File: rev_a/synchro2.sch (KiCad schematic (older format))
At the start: 26 parts, among them SW1 BUTTON_SPST, U1 AS505X, U2 AS505X, U3 LM2931, U4 MCP2562, U5 TM4C123_QFP64_SYNCHRO2, X1 10MHz

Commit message: Rev. A is pretty close to being ready.
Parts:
- removed N3: JTAG, symbol SWDEBUG_CONN
- added C22, C23: .1uF, symbol C
- added H1: M3.0_#4_HOLE_J, symbol M3.0_#4_HOLE
- added H10, H5: M1.0_HOLE, symbol M1.0_HOLE
- added H2: M3.0_#4_HOLE_K, symbol M3.0_#4_HOLE
- added H3: M3.0_#4_HOLE_L, symbol M3.0_#4_HOLE
- added H4: M3.0_#4_HOLE_M, symbol M3.0_#4_HOLE
- added H6: M3.5_#6_HOLE_N, symbol M3.5_#6_HOLE
- added H7: M3.5_#6_HOLE_O, symbol M3.5_#6_HOLE
- added H8: M3.5_#6_HOLE_P, symbol M3.5_#6_HOLE
- added H9: M3.5_#6_HOLE_Q, symbol M3.5_#6_HOLE
- added J1: UPDATE_ENABLE, symbol EN_DIS_JUMPER
- added N3, N4: ARM_JTAG_10PIN, symbol ARM_JTAG_10PIN
- added TP1: L5.0V, symbol TEST_POINT
- added TP13: MB_TX, symbol TEST_POINT
- added TP14: MB_RX, symbol TEST_POINT
- added TP15: ENC_INT, symbol TEST_POINT
- added TP16: DR_SCLK, symbol TEST_POINT
- added TP17: DR_SEL, symbol TEST_POINT
- added TP18: DR_MISO, symbol TEST_POINT
- added TP19: DR_MOSI, symbol TEST_POINT
- added TP2: L3.3V, symbol TEST_POINT
- added TP3: LGND, symbol TEST_POINT
- C1: value C -> 22uF
- C2, C5, C6, C7, C8: value .1 -> .1uF
- C4: renamed from C3; value .1 -> .1uF
- D1: value LED_VERT -> R971-KN-1
- R2: value R_VERT -> 10K
- SW1: value BUTTON_SPST -> RESET_BUTTON
- U1, U2: value AS505X -> AS5050
- U5: value TM4C123_QFP64_SYNCHRO2 -> TM4C123GH6PM
- U6: renamed from U?; value TC101X -> TC1015
- gave numbers to parts that had none: 1
- renumbered C9 to C11, C11 to C12, C4 to C3
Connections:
- net 3.3V: now also C22.1, C23.1, N3.1 (VCC), N4.1 (VCC), TP2.1 (TESTPOINT)
- net 5V: now also TP1.1 (TESTPOINT)
- net GND: now also C22.2, C23.2, J1.2 (GND), N3.3 (GND), N3.5 (GND), N3.9 (GNDDETECT), N4.3 (GND), N4.5 (GND), N4.9 (GNDDETECT), TP3.1 (TESTPOINT)
- net Motor_Power/MB_PWM_CLK: now also U5.57 (PB5/CAN0Tx/SSI2Fss/T1CCP1); no longer U5.58 (PB4/CAN0Rx/SSI2Clk/T1CCP0)
- net MB_RX: now reaches U5.59 (PE4/CAN0Rx/U5Rx)
- net MB_RX: now also U4.4 (RXD), TP14.1 (TESTPOINT); no longer U4.1 (TXD)
- net MB_TX: now reaches U5.60 (PE5/CAN0Tx/U5Tx)
- net MB_TX: now also U4.1 (TXD), TP13.1 (TESTPOINT); no longer U4.4 (RXD)
- net at U4.8 (STBY): now also U5.58 (PB4/CAN0Rx/SSI2Clk/T1CCP0); no longer U5.24 (PA7)
- net SEL_FB: now reaches U5.43 (PD4/U6Rx/WT4CCP0)
- net SEL_FB: now also N1.14 (SEL1); no longer N1.13 (SEL0)
- net SEL_LR: now reaches U5.44 (PD5/U6Tx/WT4CCP1)
- net SEL_LR: now also N1.13 (SEL0); no longer N1.14 (SEL1)
- net TW_MOSI: now reaches U1.1 (MOSI), U5.22 (PA5/SSI0Tx)
- net at U1.15 (~INT), U5.1 (PB6/SSI2Rx/T0CCP0): now also TP15.1 (TESTPOINT)
- net TW_MISO: now reaches U1.2 (MISO), U5.21 (PA4/SSI0Rx)
- net TW_SCK: now reaches U1.3 (SCK), U5.19 (PA2/SSI0Clk)
- net ~TW_SEL: now reaches U1.4 (~SS), U5.20 (PA3/SSI0Fss)
- net DR_MOSI: now reaches U2.1 (MOSI), U5.29 (PF1/SSI1Tx/T0CCP1/U1CTS)
- net DR_MOSI: now also TP19.1 (TESTPOINT)
- net DR_MISO: now reaches U2.2 (MISO), U5.28 (PF0/CAN0Rx/SSI1Rx/T0CCP0/U1RTS)
- net DR_MISO: now also TP18.1 (TESTPOINT)
- net DR_SCLK: now reaches U2.3 (SCK), U5.30 (PF2/SSI1Clk/T1CCP0)
- net DR_SCLK: now also TP16.1 (TESTPOINT)
- net ~DR_SEL: now reaches U2.4 (~SS), U5.31 (PF3/CAN0Tx/SSI1Fss/T1CCP1)
- net ~DR_SEL: now also TP17.1 (TESTPOINT)
- net UART_RX: now reaches N2.4 (TXD_ORANGE), U5.17 (PA0/CAN1Rx/U0Rx)
- net UART_TX: now reaches N2.5 (RXD_YELLOW), U5.18 (PA1/CAN1Tx/U0Tx)
- net TCK: now reaches U5.52 (PC0/SWCLK/TCK)
- net TCK: now also N3.4 (SWDCLK/TCK), N4.4 (SWDCLK/TCK)
- net TMS: now reaches U5.51 (PC1/SWDIO/TMS)
- net TMS: now also N3.2 (SWDIO/TMS), N4.2 (SWDIO/TMS)
- net TDI: now reaches U5.50 (PC2/TDI)
- net TDI: now also N3.8 (NC/TDI), N4.8 (NC/TDI)
- net TDO: now reaches U5.49 (PC3/SWO/TDO)
- net TDO: now also N3.6 (SWO/TDO), N4.6 (SWO/TDO)
- net at U5.15 (PC5/U1CTS/U1Tx/U4Tx/WT0CCP1): now also J1.1 (ENABLE)
- net ~RESET: now reaches R2.1, SW1.1, U5.38 (~RST)
- net ~RESET: now also N3.10 (~RESET), N4.10 (~RESET)
- net Motor_Power/MB_DAC_CLK renamed DAC_CLK
- net Motor_Power/MB_DR_EN1 renamed DR_EN1
- net Motor_Power/MB_DR_EN2 renamed DR_EN2
- net Motor_Power/MB_MOSI renamed DAC_MOSI
- net Motor_Power/MB_TW_EN1 renamed TW_EN1
- net Motor_Power/MB_TW_EN2 renamed TW_EN2
- net Motor_Power/~MB_DAC_SEL renamed ~DAC_SEL
- no-connect marks 33 -> 31
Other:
- note added: "35V Alum."
- note added: "6.3V Tantalum\nESR<40mOhm"
- note added: "AVX: TAJA226K006RNJ"
- note added: "C1 = KMet:\nEEV226M035A9DAA"
- note added: "DAC SPI"
- note added: "DRIVE\nSHAFT"
- note added: "Drive SPI"
- note added: "Front/Back Left/Right Select"
- note added: "J"
- note added: "JTAG"
- note added: "K"
- note added: "L"
- note added: "LG"
- note added: "M"
- note added: "MakerBus TX/RX"
- note added: "N"
- note added: "O"
- note added: "P"
- note added: "PCB Mounting Holes\n(Letter matches mech. design)"
- note added: "Q"
- note added: "TWIST\nSHAFT"
- note added: "Twist SPI"
- note added: "Twist/Drive Enables"
- note removed: "TANT\nESR<40mOhm"
- moved on the sheet: C10, C12, D1, R1, R2, SW1, X1

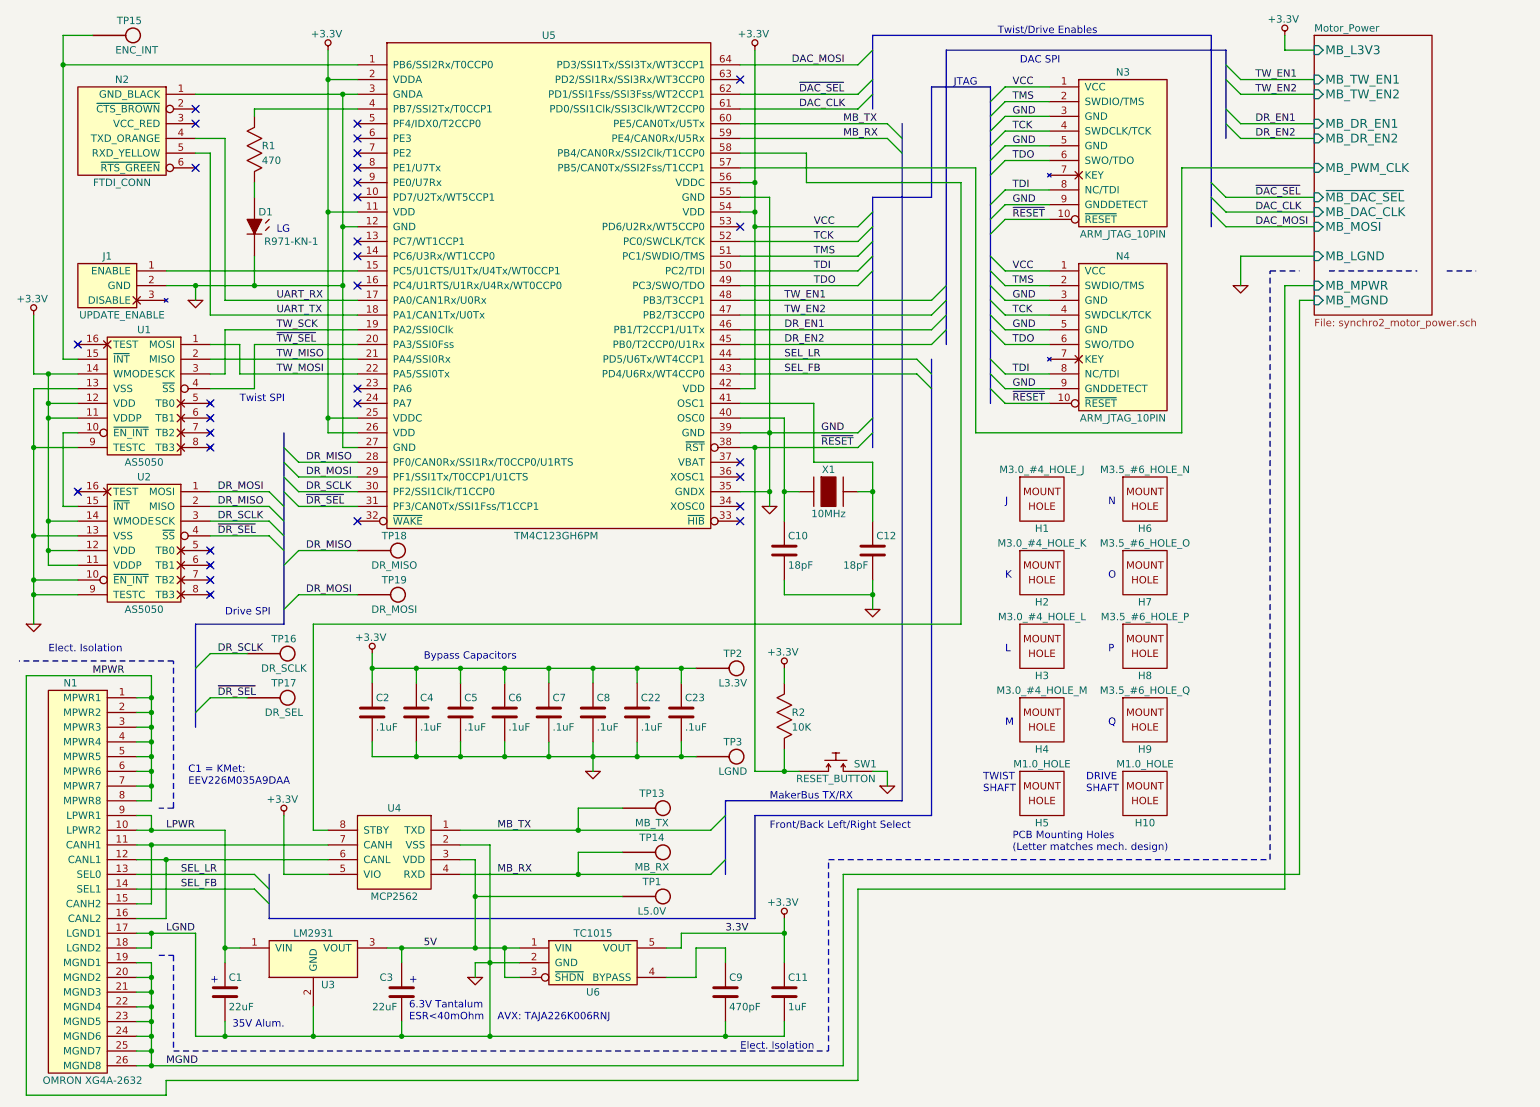
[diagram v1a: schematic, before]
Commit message: Tweak compennt values to match pricing database.  No footprints were changed.
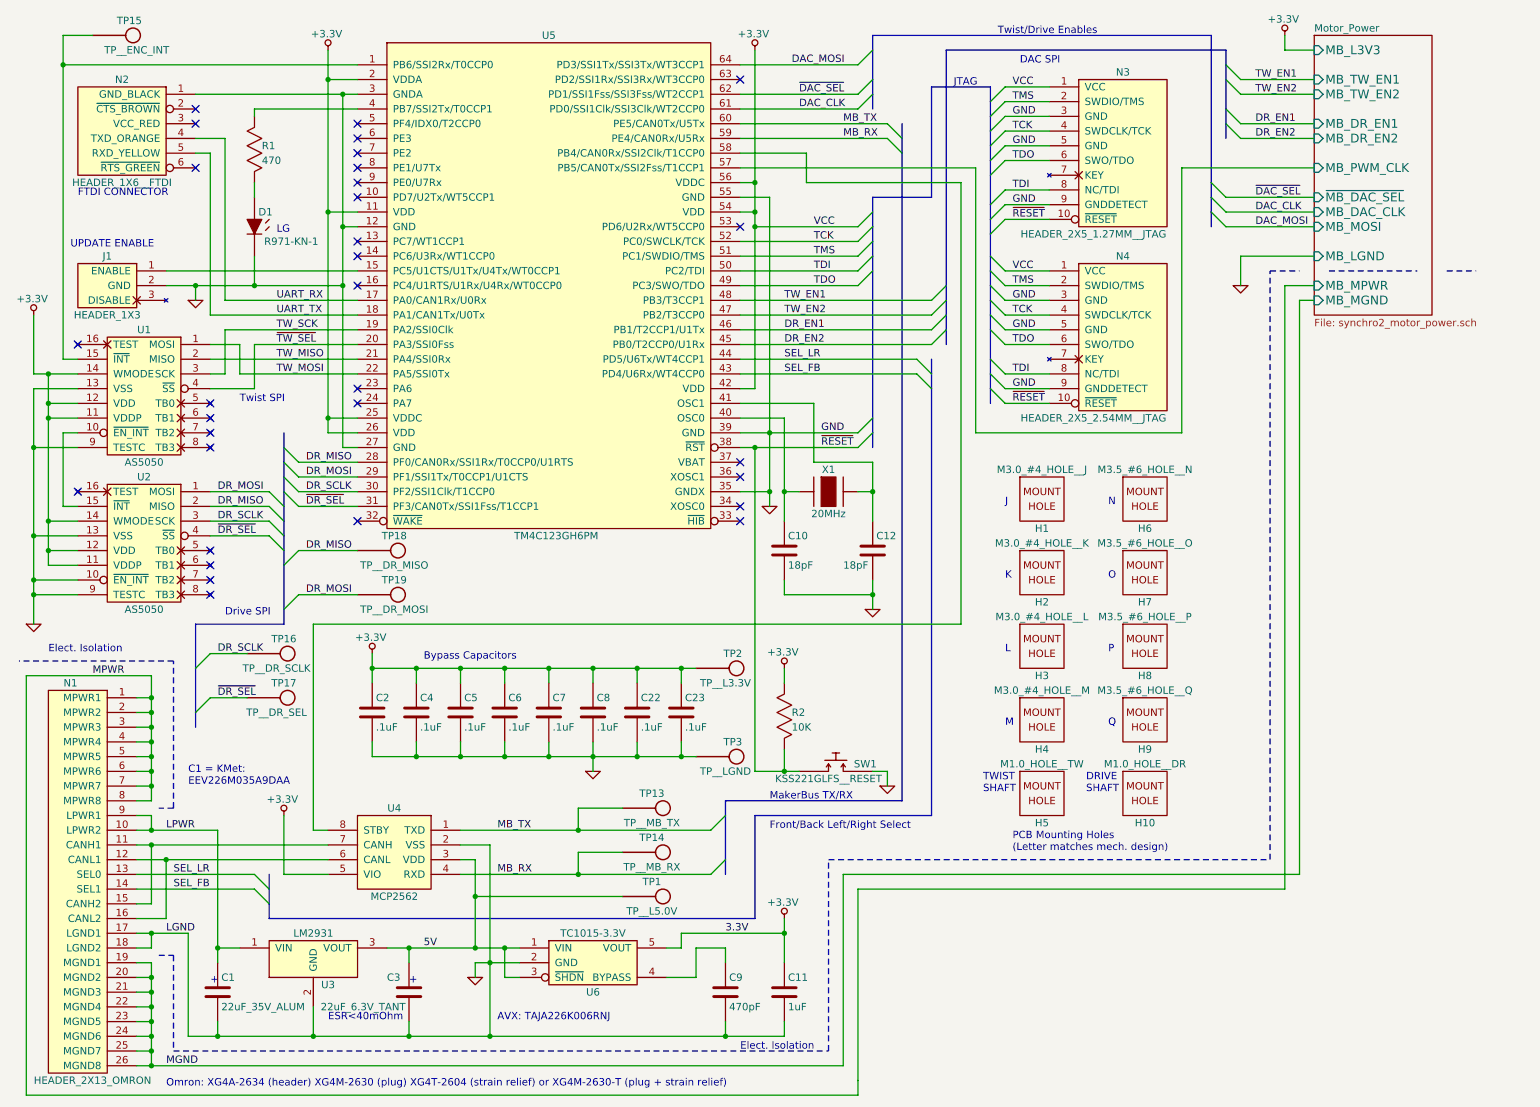
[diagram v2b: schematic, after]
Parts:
- C1: value 22uF -> 22uF_35V_ALUM
- C3: value 22uF -> 22uF_6.3V_TANT
- H1: value M3.0_#4_HOLE_J -> M3.0_#4_HOLE__J
- H10: value M1.0_HOLE -> M1.0_HOLE__DR
- H2: value M3.0_#4_HOLE_K -> M3.0_#4_HOLE__K
- H3: value M3.0_#4_HOLE_L -> M3.0_#4_HOLE__L
- H4: value M3.0_#4_HOLE_M -> M3.0_#4_HOLE__M
- H5: value M1.0_HOLE -> M1.0_HOLE__TW
- H6: value M3.5_#6_HOLE_N -> M3.5_#6_HOLE__N
- H7: value M3.5_#6_HOLE_O -> M3.5_#6_HOLE__O
- H8: value M3.5_#6_HOLE_P -> M3.5_#6_HOLE__P
- H9: value M3.5_#6_HOLE_Q -> M3.5_#6_HOLE__Q
- J1: value UPDATE_ENABLE -> HEADER_1X3
- N1: value OMRON XG4A-2632 -> HEADER_2X13_OMRON
- N2: value FTDI_CONN -> HEADER_1X6__FTDI
- N3: value ARM_JTAG_10PIN -> HEADER_2X5_1.27MM__JTAG
- N4: value ARM_JTAG_10PIN -> HEADER_2X5_2.54MM__JTAG
- SW1: value RESET_BUTTON -> KSS221GLFS__RESET
- TP1: value L5.0V -> TP__L5.0V
- TP13: value MB_TX -> TP__MB_TX
- TP14: value MB_RX -> TP__MB_RX
- TP15: value ENC_INT -> TP__ENC_INT
- TP16: value DR_SCLK -> TP__DR_SCLK
- TP17: value DR_SEL -> TP__DR_SEL
- TP18: value DR_MISO -> TP__DR_MISO
- TP19: value DR_MOSI -> TP__DR_MOSI
- TP2: value L3.3V -> TP__L3.3V
- TP3: value LGND -> TP__LGND
- U6: value TC1015 -> TC1015-3.3V
- X1: value 10MHz -> 20MHz
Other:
- note added: "ESR<40mOhm"
- note added: "FTDI CONNECTOR"
- note added: "Omron: XG4A-2634 (header) XG4M-2630 (plug) XG4T-2604 (strain relief) or XG4M-2630-T (plug + strain relief)\n"
- note added: "UPDATE ENABLE"
- note removed: "35V Alum."
- note removed: "6.3V Tantalum\nESR<40mOhm"
- moved on the sheet: C1, C3
